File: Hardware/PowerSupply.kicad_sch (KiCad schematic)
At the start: 19 parts

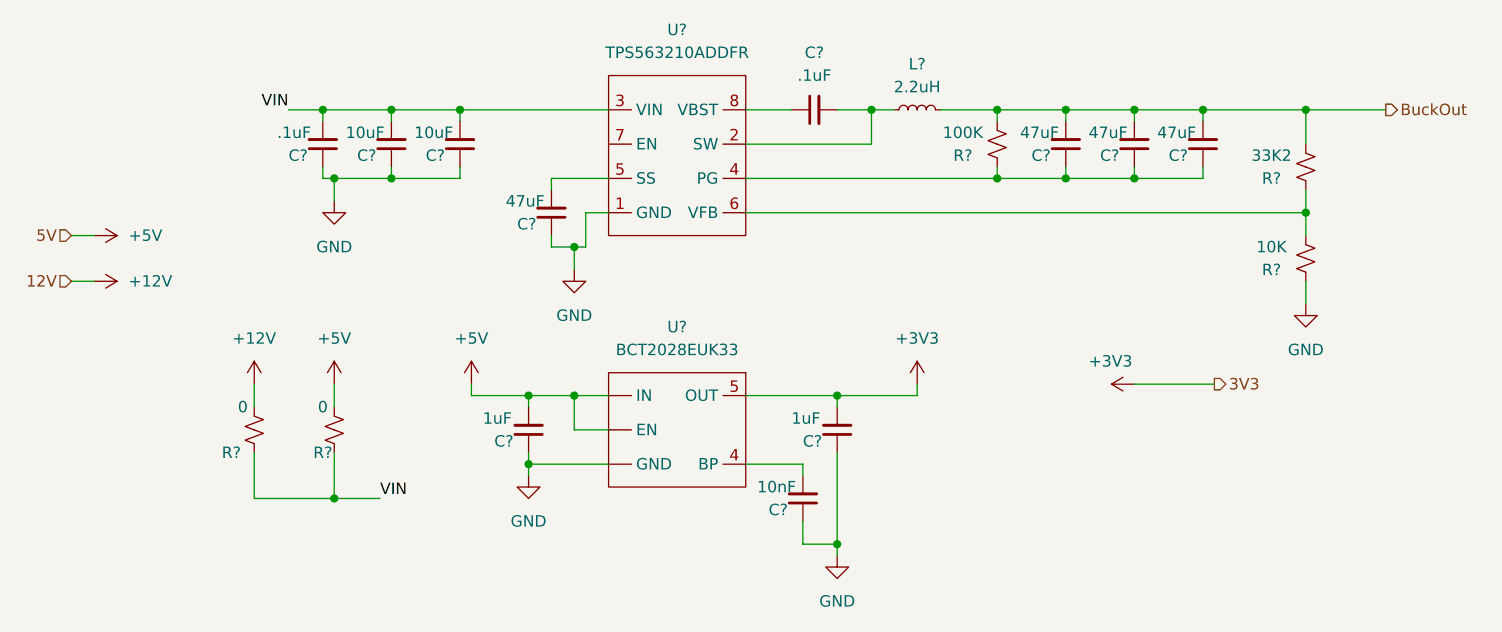
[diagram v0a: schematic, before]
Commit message: Finished Schematics and placed most components
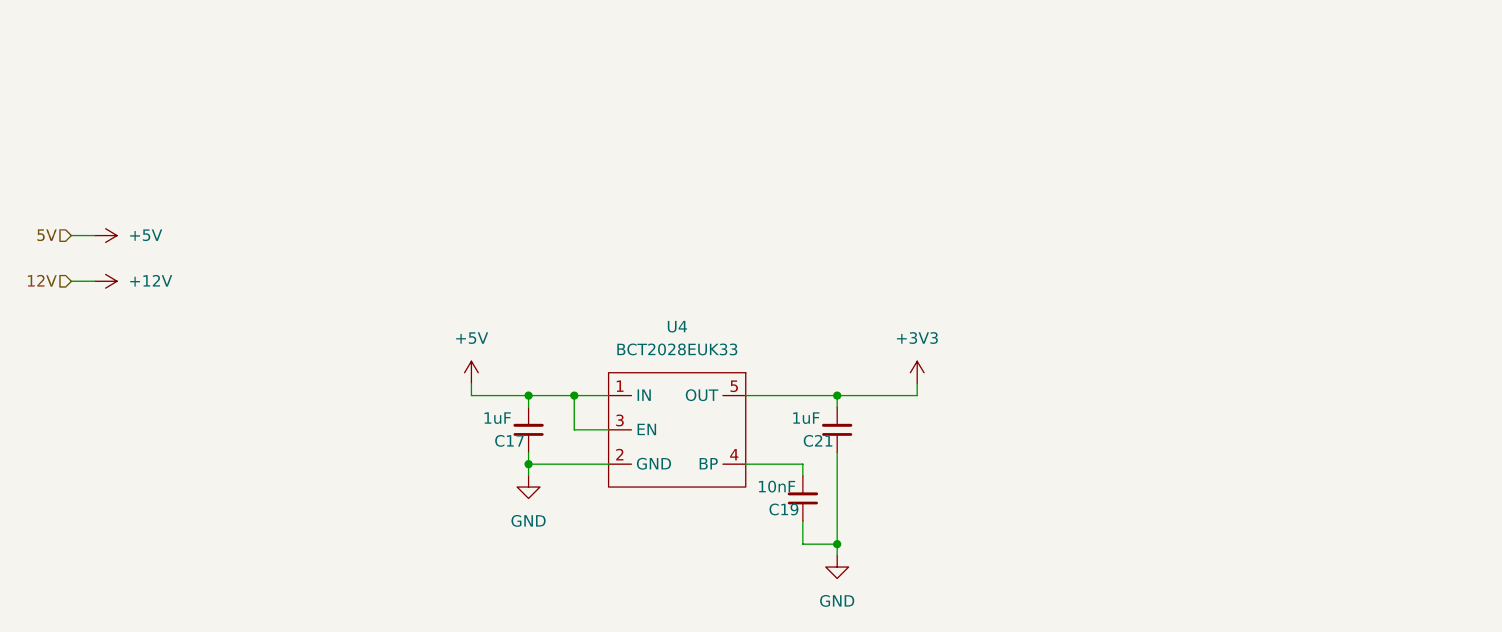
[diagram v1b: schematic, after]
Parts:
- removed C? (x4): 47uF, Capacitor_SMD:C_1210_3225Metric_Pad1.33x2.70mm_HandSolder, symbol Device:C_Small
- removed C? (x2): .1uF, Capacitor_SMD:C_0603_1608Metric_Pad1.08x0.95mm_HandSolder, symbol Device:C_Small
- removed C? (x2): 10uF, Capacitor_SMD:C_1206_3216Metric_Pad1.33x1.80mm_HandSolder, symbol Device:C_Small
- removed L?: 2.2uH, symbol Device:L_Small
- removed R?: 10K, Resistor_SMD:R_0402_1005Metric_Pad0.72x0.64mm_HandSolder, symbol Device:R_Small_US
- removed R?: 100K, Resistor_SMD:R_0402_1005Metric_Pad0.72x0.64mm_HandSolder, symbol Device:R_Small_US
- removed R? (x2): 0, Resistor_SMD:R_0805_2012Metric_Pad1.20x1.40mm_HandSolder, symbol Device:R_Small_US
- removed R?: 33K2, Resistor_SMD:R_0402_1005Metric_Pad0.72x0.64mm_HandSolder, symbol Device:R_Small_US
- removed U?: TPS563210ADDFR, symbol POWER_:TPS563210ADDFR
- U4: renamed from U?; footprint (none) -> Package_TO_SOT_SMD:SOT-23-5_HandSoldering
- gave numbers to parts that had none: 3
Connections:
- net +5V: now also U4.1 (IN), U4.3 (EN); no longer U4. (IN)
- net GND: now also U4.2 (GND); no longer U4. (IN)
